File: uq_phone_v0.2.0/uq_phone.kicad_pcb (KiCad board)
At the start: 6 copper layers, 45 x 108 mm, 187 parts, among them J1 PJ-605-6A, J2 124018312112A, J3 BM03B-ACHSS-GAN-TF_LF__SN_, J6 Conn_ARM_SWD_TagConnect_TC2030, J7 559092474, J8 MCS-302S-C1, J9 559092474, M1 C08-00A, Q1 MMBT3904LP-7, Q2 MMBT3904LP-7, Q3 S8050, SW1 SKTAAAE010, SW10 SKTAAAE010, SW11 SKTAAAE010, SW12 SKTAAAE010, SW13 SKTAAAE010, SW14 SKTAAAE010, SW15 SKTAAAE010, SW16 SKSCLCE010, SW17 SKTAAAE010, SW18 SKTAAAE010, SW19 SKTAAAE010, SW2 SKTAAAE010, SW20 SKTAAAE010, SW21 SKTAAAE010, SW22 SKSCLCE010, SW23 SKTAAAE010, SW24 SKTAAAE010, SW25 SKTAAAE010, SW26 SKTAAAE010, SW27 SKTAAAE010, SW28 SKTAAAE010, SW29 SKTAAAE010, SW3 SKTAAAE010, SW30 SKTAAAE010, SW31 SKTAAAE010, SW32 SKTAAAE010, SW33 SKTAAAE010, SW34 SKTAAAE010, SW35 SKTAAAE010, SW36 SKTAAAE010, SW37 SKTAAAE010, SW38 SKTAAAE010, SW39 SKTAAAE010, SW4 SKTAAAE010, SW40 SKTAAAE010, SW41 SKTAAAE010, SW5 SKTAAAE010, SW6 SKSCLCE010, SW7 SKTAAAE010, SW8 SKTAAAE010, SW9 SKTAAAE010, U1 TPS62162DSGR, U10 TPD8F003DQDR, U11 LSM6DSVTR, U12 DRV2603RUNR, U13 TS3A5018RSVR, U14 NAU88C22YG, U15 TPS22964CYZPR, U17 TXU0204DTRR, U18 TXU0304DTRR, U19 TXU0104DTRR, U2 MCP73871-2CCI_ML, U20 TXU0104DTRR, U3 BQ27441DRZR-G1A, U5 TCA9509MRVHR, U6 STM32H723VGHx, U8 TPD3F303DQDR, U9 AZV5001RA4-7

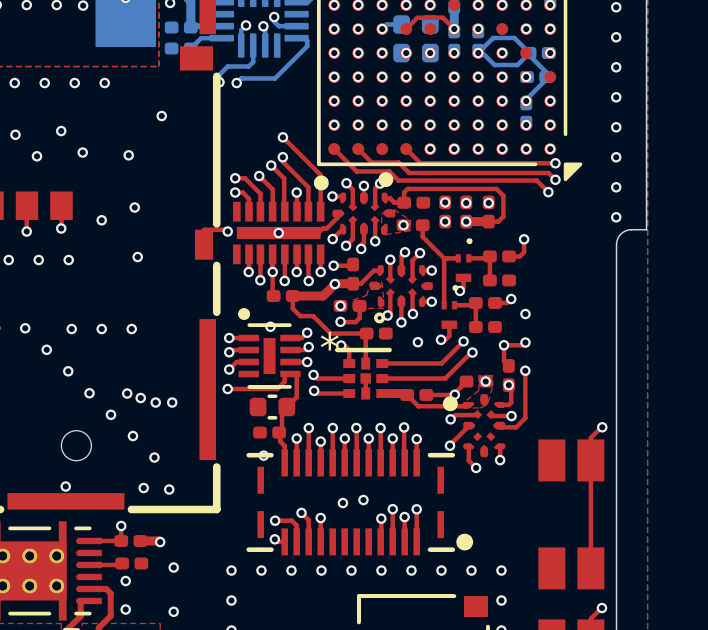
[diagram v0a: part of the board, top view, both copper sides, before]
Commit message: Fix KiCad libraries and update soft power circuit
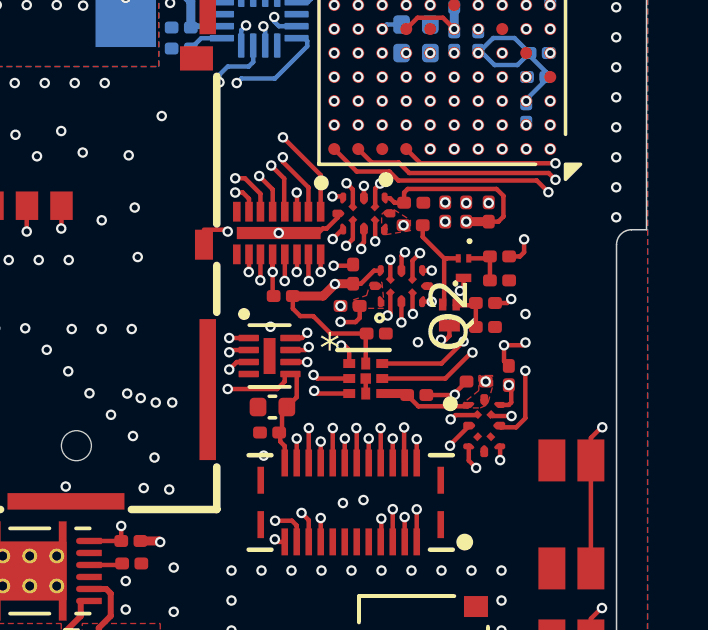
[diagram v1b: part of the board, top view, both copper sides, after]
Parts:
- Q2: footprint MMBT3904LP-7:DFN101X61X53-3N -> MMBT3904LP-7:MMBT3904LP7
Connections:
- C1 pad 2: MCP_OUT -> REG_VIN_SW
- J8 pad 21: uSD_SIM_CD -> uSD_TRAY_DET
- J8 pad 4: +3.3V -> SD_VDD_SW
- R25 pad 1: uSD_SIM_CD -> uSD_TRAY_DET
- U1 pad 2: MCP_OUT -> REG_VIN_SW
- U1 pad 3: MCP_OUT -> REG_VIN_SW
- U10 pad 12: uSD_SIM_CD -> uSD_TRAY_DET
- U6 pad G5: unconnected-(U6-PB2-PadG5) -> MCU_PWR_LATCH
- U6 pad J7: unconnected-(U6-PB10-PadJ7) -> SD_PWR_EN
- U6 pad K7: unconnected-(U6-PB11-PadK7) -> uSD_TRAY_DET
- U6 pad K8: PB_PWR -> PWR_BUTTON_SENSE
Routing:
- net uSD_TRAY_DET: track 0.00 -> 4.87 mm, vias 0 -> 3
- net uSD_SIM_CD: track 4.87 -> 0.00 mm, vias 2 -> 0
- net unconnected-(U6-PB11-PadK7): vias 1 -> 0

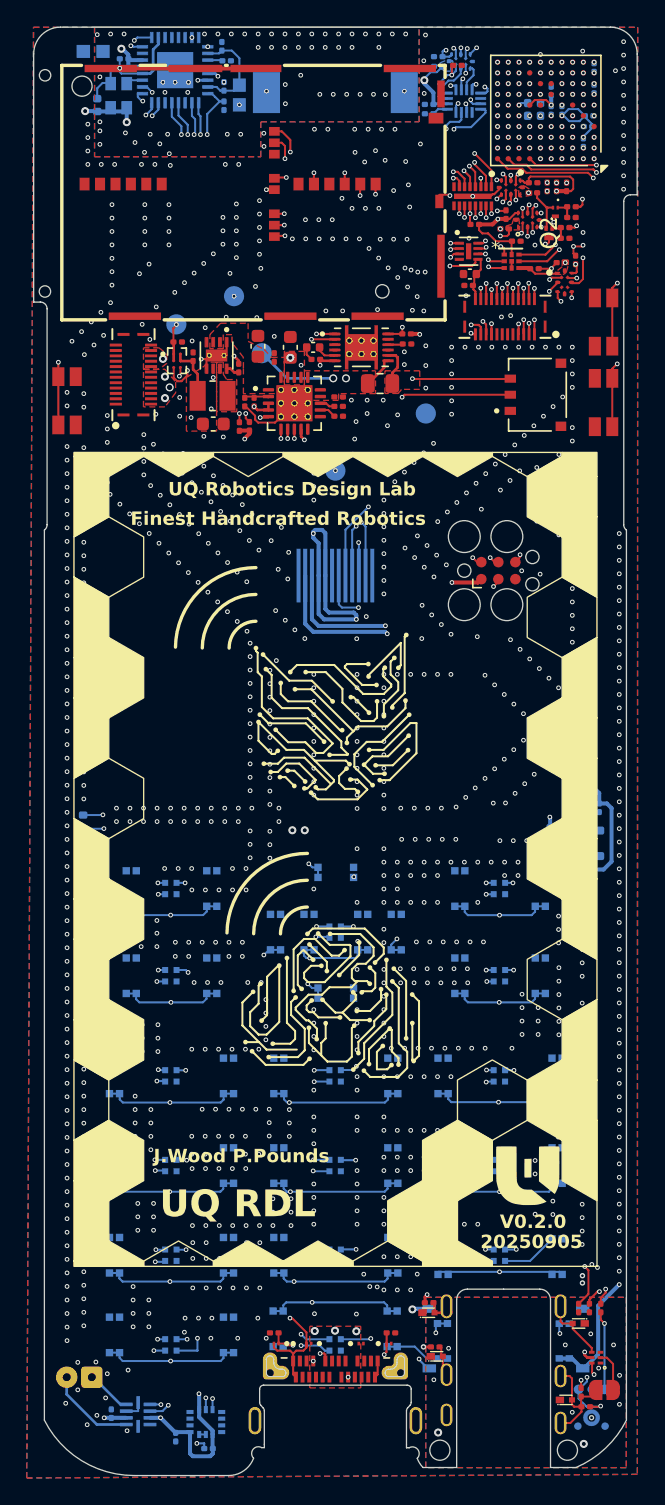
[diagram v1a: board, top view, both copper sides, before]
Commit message: Route soft power switch
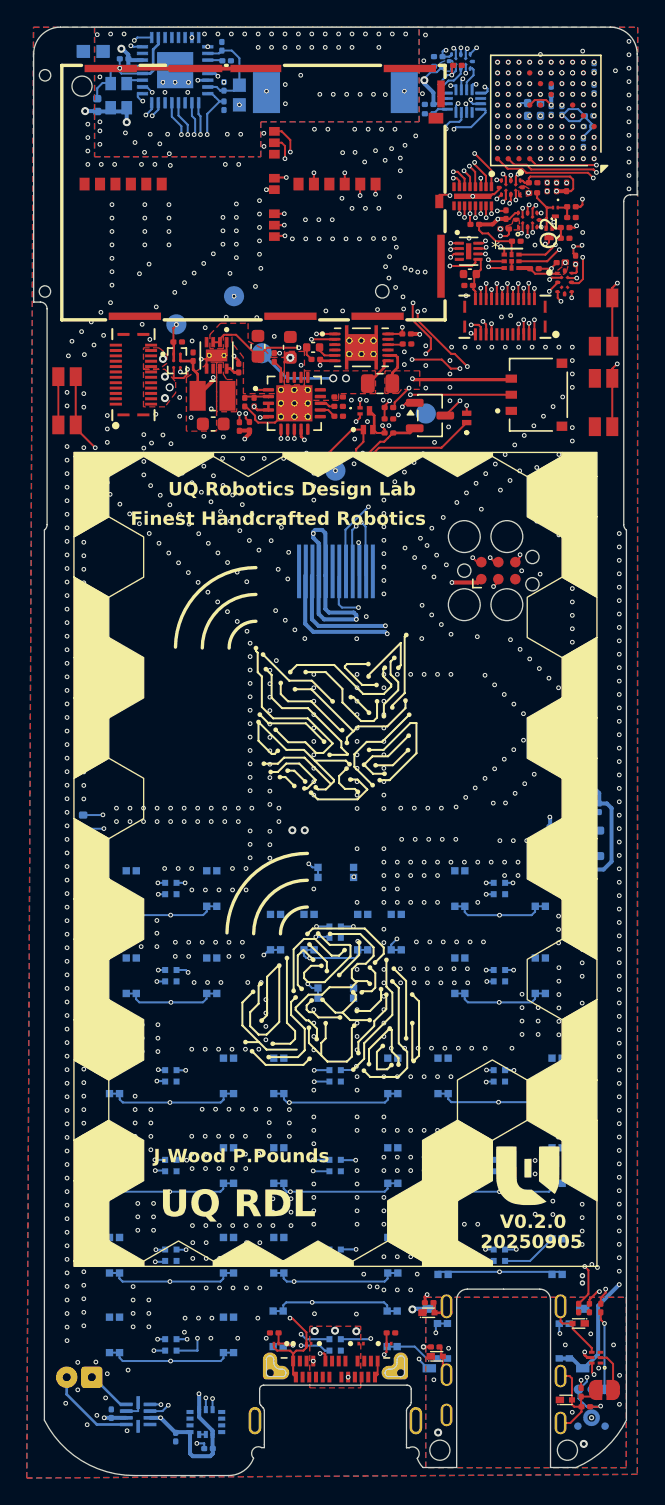
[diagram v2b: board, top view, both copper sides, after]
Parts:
- added D12: BAT54LP-7, BAT54LP-7:DESD3V3S1BL7B, F.Cu at (50.5, 50.4)
- added D2: BAT54LP-7, BAT54LP-7:DESD3V3S1BL7B, F.Cu at (42.9, 50.9)
- added Q4: DMP2035U-7, Package_TO_SOT_SMD:SOT-23-3, F.Cu at (47.8, 49.9)
- added Q5: MMBT3904LP-7, MMBT3904LP-7:MMBT3904LP7, F.Cu at (43.0, 49.5)
- added R30: 100k, Resistor_SMD:R_0201_0603Metric, F.Cu at (44.8, 51.1)
- added R31: 4.7k, Resistor_SMD:R_0201_0603Metric, F.Cu at (44.8, 49.2)
- added R34: 47k, Resistor_SMD:R_0201_0603Metric, F.Cu at (44.8, 50.1)
- moved DISP1 0.31 mm to (40.8, 53.6)
- moved J3 0.08 mm to (55.8, 48.3)
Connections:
- SW22 pad 1: PB_PWR -> GND
- SW22 pad 2: PB_PWR -> GND
- SW22 pad 3: GND -> Net-(D12-K)
- SW22 pad 4: GND -> Net-(D12-K)
- U6 pad G5: MCU_PWR_LATCH -> unconnected-(U6-PB2-PadG5)
- U6 pad J4: unconnected-(U6-PB0-PadJ4) -> MCU_PWR_LATCH
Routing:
- net PB_PWR: track 52.9 -> 0.00 mm, vias 2 -> 0
- net MCU_PWR_LATCH: track 0.00 -> 42.4 mm, vias 0 -> 5
- net Net-(D12-K): track 0.00 -> 38.7 mm, vias 0 -> 2
- net PWR_BUTTON_SENSE: track 0.00 -> 35.2 mm, vias 0 -> 4
- net REG_VIN_SW: track 0.00 -> 24.3 mm, vias 0 -> 4
- net MCP_OUT: track 0.00 -> 22.6 mm, vias 0 -> 2
- net Net-(D2-A): track 0.00 -> 6.44 mm, vias 0 -> 2
- net GND: track 81.3 -> 86.5 mm, vias 1002 -> 1012
- net Net-(Q5-Pad1): track 0.00 -> 4.70 mm, vias 0 -> 2
- net +3.3V: track 237.9 -> 239.7 mm
- net HP_DET: track 85.4 -> 86.4 mm
- net unconnected-(U6-PB0-PadJ4): vias 1 -> 0
- net DISP_BL: vias 3 -> 4

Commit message: Update PCB routing
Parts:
- added C22: 1uF, Capacitor_SMD:C_0201_0603Metric, F.Cu at (51.3, 45.9)
- added C23: 1uF, Capacitor_SMD:C_0201_0603Metric, F.Cu at (52.1, 45.9)
- added Q6: MMBT3904LP-7, MMBT3904LP-7:MMBT3904LP7, F.Cu at (51.9, 50.2)
- added R29: 100k, Resistor_SMD:R_0201_0603Metric, F.Cu at (51.9, 47.7)
- added R37: 10k, Resistor_SMD:R_0201_0603Metric, F.Cu at (51.9, 48.8)
- added U7: TPS22964CYZPR, TPS22964CYZPR:IC_SN74LVC2G34YZPR, F.Cu at (58.0, 43.0)
